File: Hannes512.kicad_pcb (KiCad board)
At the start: 2 copper layers, 54.3 x 72.2 mm, 23 parts, among them J0 TED_SOCKET, J1 CONN_CS, J2 RAM_SELECTOR, U1 MOS_7360_TED, U2 AS6C4008, U3 74HCT02, U4 NE555, U5 74HCT573, U6 74HCT245, U7 GAL20V8

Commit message: Hannes256 -> Hannes512
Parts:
- J0: footprint Hannes256:DIP-48_W15.24mm_LongPads_ModSilkS -> Hannes512:DIP-48_W15.24mm_LongPads_ModSilkS
- V1: footprint Hannes256:cc_by_nc_sa -> Hannes512:cc_by_nc_sa
- V2: footprint Hannes256:logo -> Hannes512:logo
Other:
- board text added: "CC-BY-NC-SA © SukkoPera 2022-2023 github.com/ SukkoPera/ Hannes512"
- board text removed: "CC-BY-NC-SA © SukkoPera 2022-2023 github.com/ SukkoPera/ Hannes256"

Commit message: Ready for V1
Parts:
- C5, C6: moved to F.Cu
- U5, U6: footprint Package_SO:SOIC-20W_7.5x12.8mm_P1.27mm -> Package_SO:SO-20_5.3x12.6mm_P1.27mm
- moved V1 10.5 mm to (148.5, 128.3)
- moved C5 3.08 mm to (112.5, 81.7)
- moved C6 3.08 mm to (107.7, 81.7), turned to 0 degrees
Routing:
- net d1: track 82.8 -> 78.0 mm
- net d2: track 84.1 -> 79.8 mm
- net a16: track 72.4 -> 76.1 mm
- net +5V: track 237.2 -> 233.9 mm, vias 10 -> 9
- net a7: track 25.6 -> 28.1 mm
- net d6: track 72.5 -> 70.0 mm
- net d3: track 62.7 -> 60.2 mm
- net d4: track 64.9 -> 62.5 mm
- net d7: track 78.8 -> 76.4 mm
- net d5: track 68.9 -> 66.5 mm
- net a10: track 41.9 -> 44.3 mm
- net d0: track 79.0 -> 76.6 mm
- net /~RAS~/~CAS~ Generation/~cs_ramrd: track 57.7 -> 55.6 mm
- net a15: track 44.5 -> 46.6 mm
- net p6: track 46.6 -> 44.6 mm
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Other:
- board text added: "CC-BY-NC-SA © SukkoPera 2023 github.com/ SukkoPera/ Hannes512"
- board text added: "V1"
- board text removed: "CC-BY-NC-SA © SukkoPera 2022-2023 github.com/ SukkoPera/ Hannes512"
- board text removed: "V4"

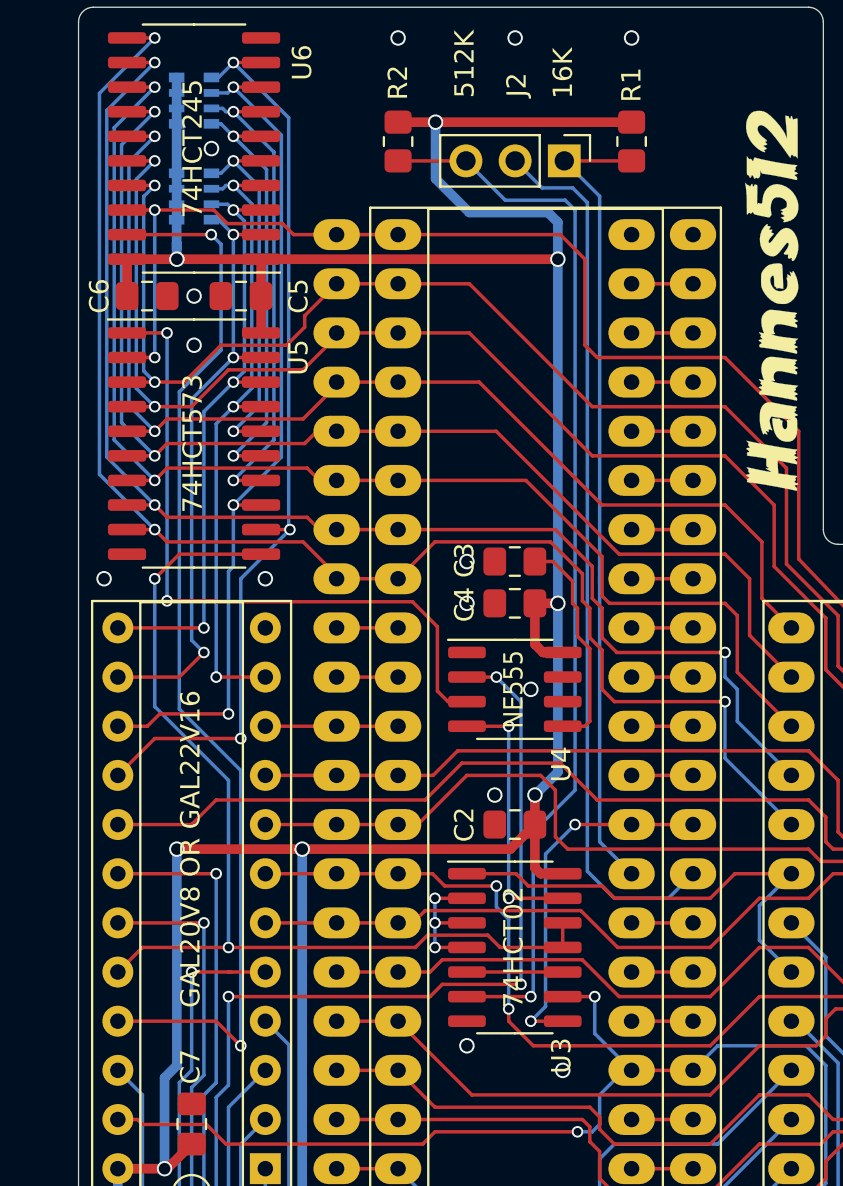
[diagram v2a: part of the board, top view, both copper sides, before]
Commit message: Some rerouting
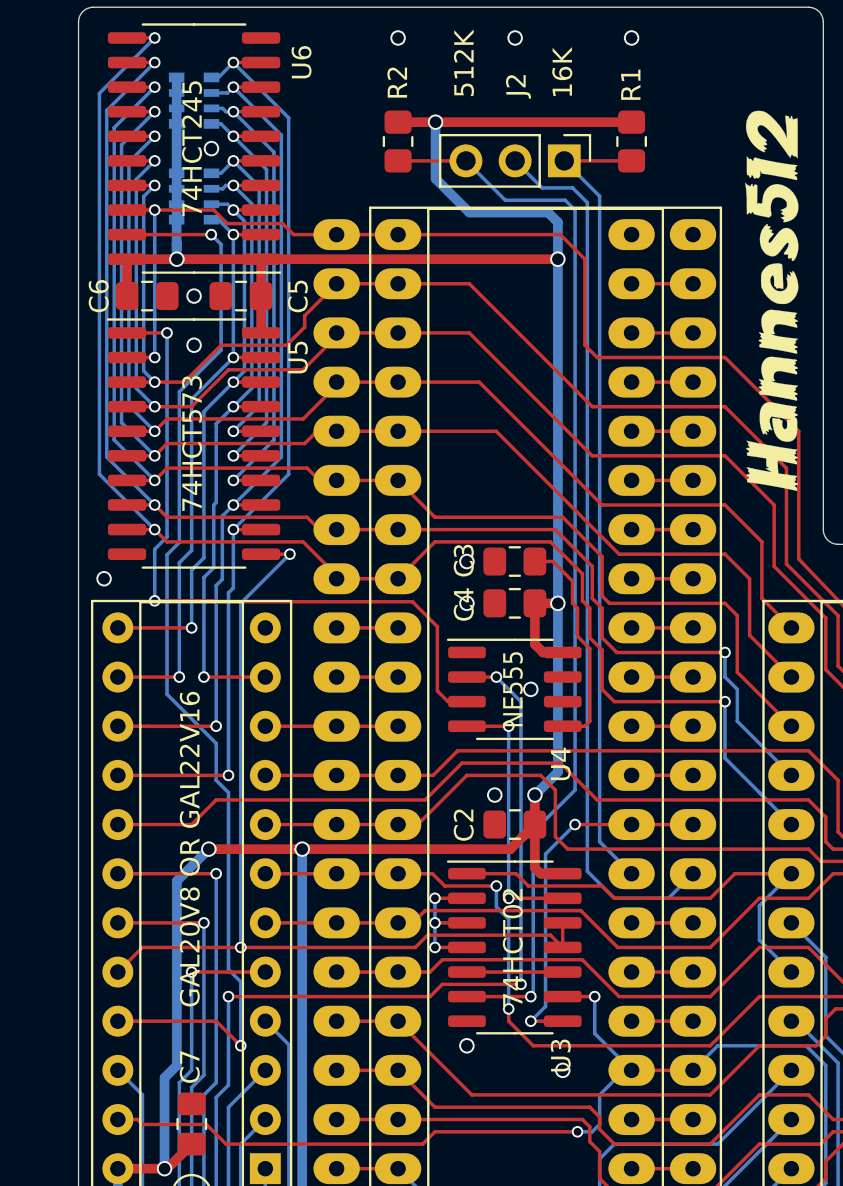
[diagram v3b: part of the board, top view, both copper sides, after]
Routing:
- net /~RAS~/~CAS~ Generation/cs_ramwr: track 52.0 -> 48.2 mm
- net +5V: track 233.9 -> 232.9 mm
- net /~RAS~/~CAS~ Generation/~u3enable: track 36.1 -> 37.0 mm
- net p2: track 33.2 -> 34.1 mm
- net p7: track 48.7 -> 49.3 mm
- net /~RAS~/~CAS~ Generation/~cs_ramrd: track 55.6 -> 56.1 mm
- net p0: track 32.0 -> 31.5 mm
- net GND: vias 26 -> 25

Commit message: More rerouting
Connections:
- net Net-(U3-Pad13) renamed /~RAS~/~CAS~ Generation/~cs_ramwr
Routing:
- net d0: track 76.6 -> 74.0 mm
- net /~RAS~/~CAS~ Generation/~cs_ramrd: track 56.1 -> 53.6 mm
- net +5V: track 232.9 -> 235.0 mm

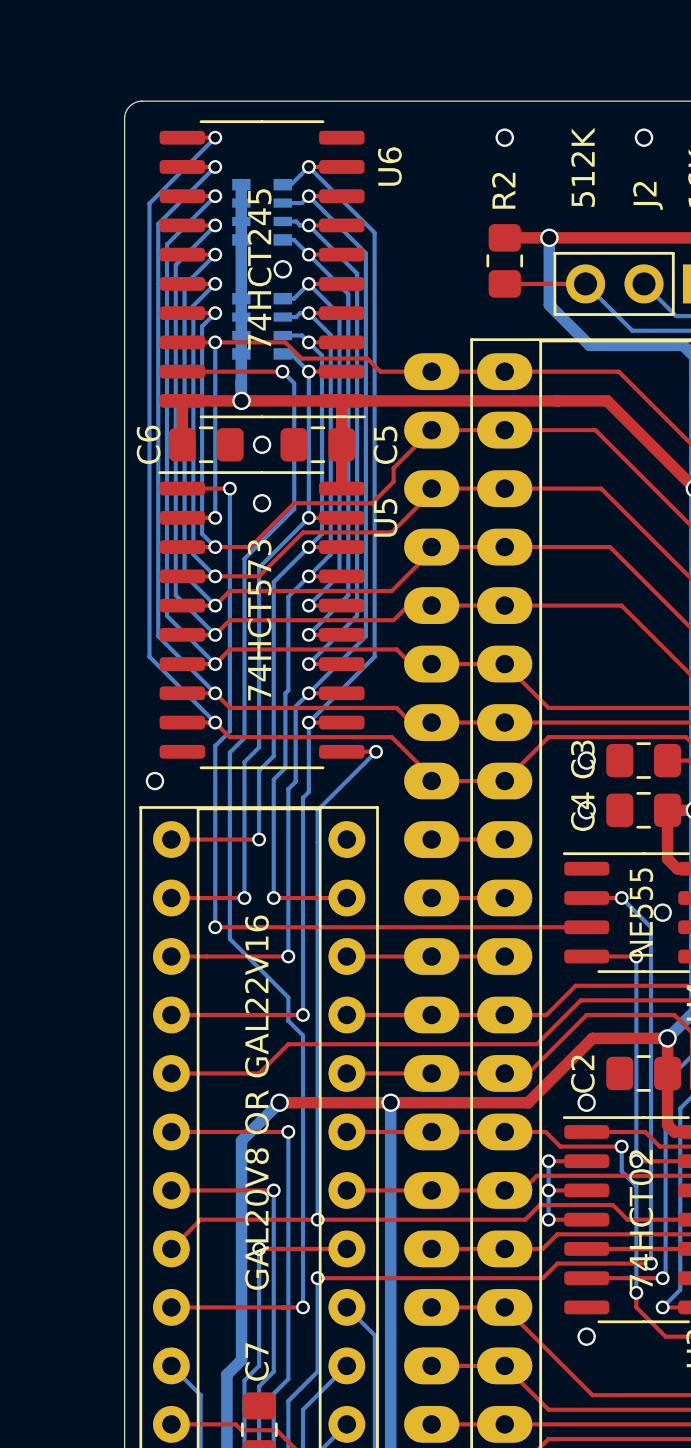
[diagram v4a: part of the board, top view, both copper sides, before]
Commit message: Relocate RN1/2 on top
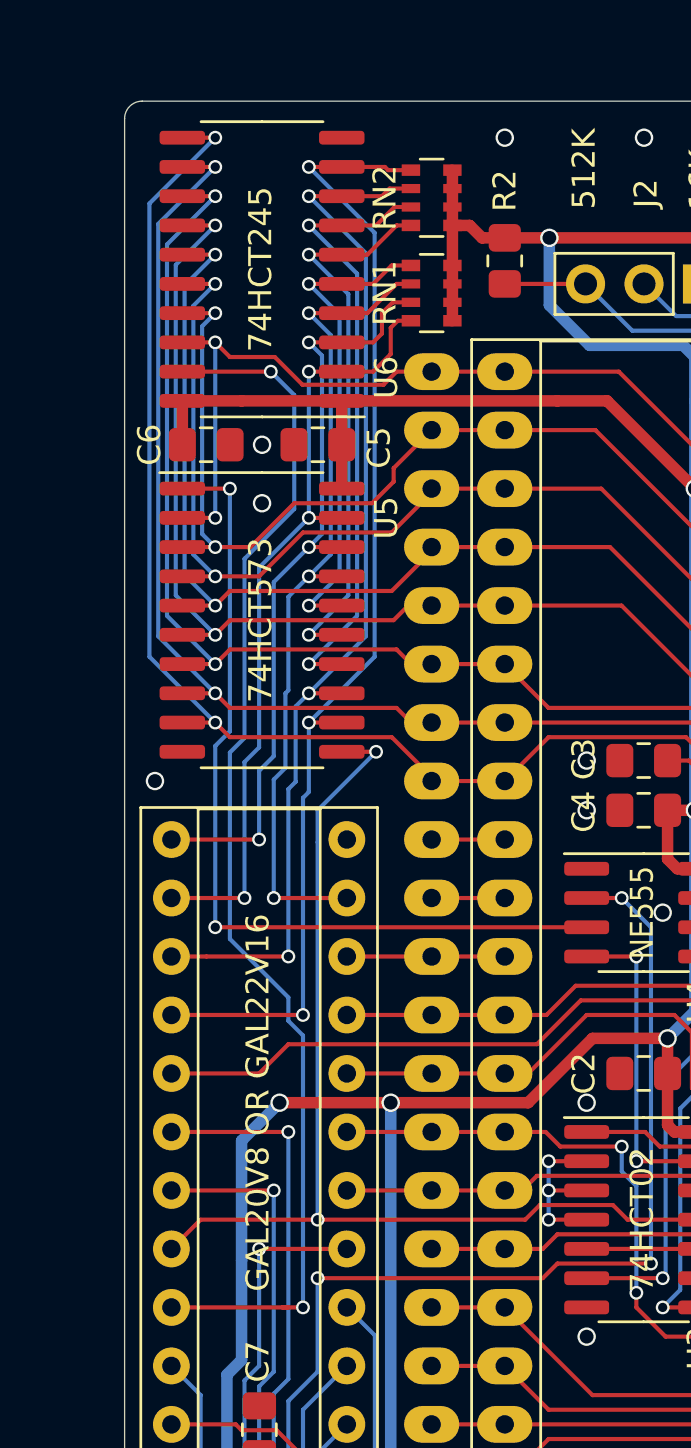
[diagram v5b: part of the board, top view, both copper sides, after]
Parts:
- RN1, RN2: moved to F.Cu
- moved RN1 7.51 mm to (117.5, 75.1), turned to 0 degrees
- moved RN2 7.39 mm to (117.5, 70.9), turned to 0 degrees
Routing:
- net p0: track 31.5 -> 34.6 mm
- net p1: track 30.9 -> 33.9 mm
- net p2: track 34.1 -> 36.4 mm
- net p5: track 24.9 -> 27.0 mm
- net p4: track 22.2 -> 24.3 mm
- net p3: track 19.3 -> 21.3 mm
- net p6: track 44.6 -> 46.5 mm
- net p7: track 49.3 -> 50.9 mm
- net +5V: track 235.0 -> 234.3 mm, vias 9 -> 8
- net GND: vias 25 -> 24

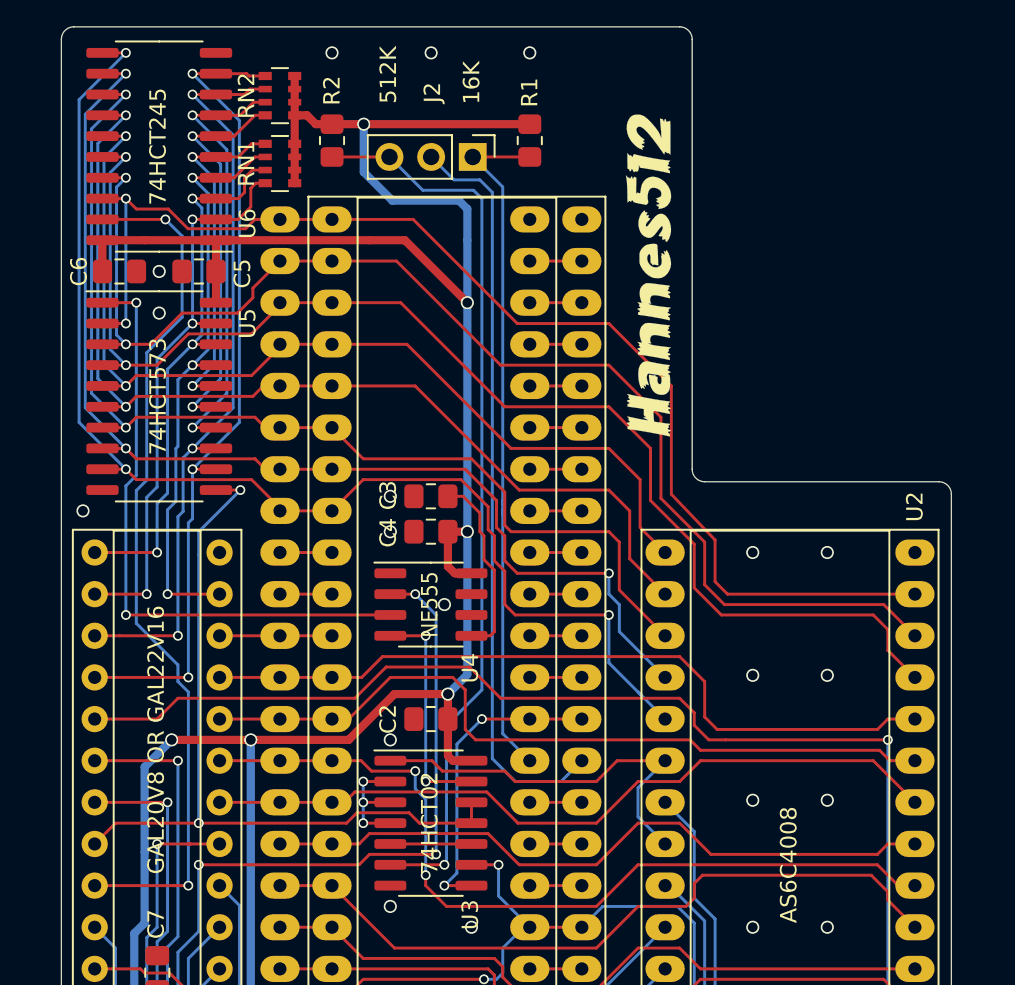
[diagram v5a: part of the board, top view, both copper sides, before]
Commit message: Add TED Kx Protection
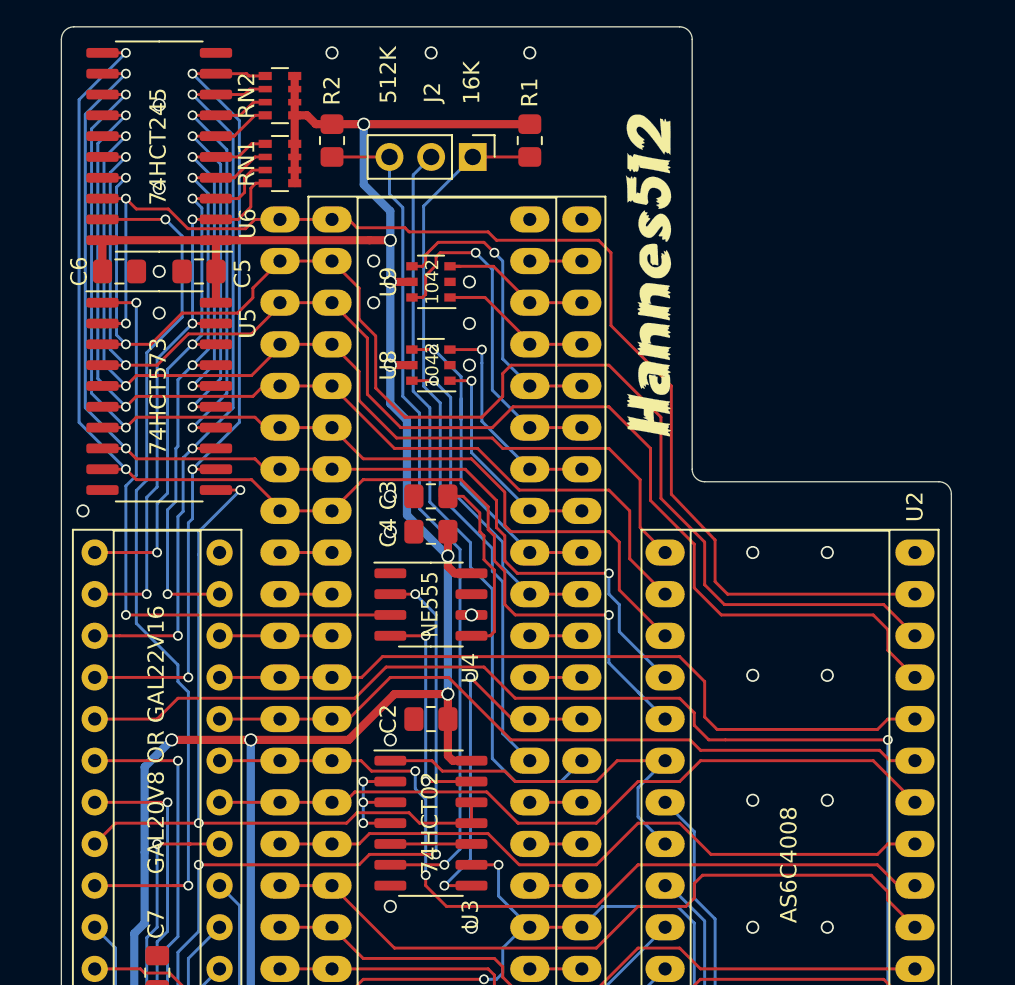
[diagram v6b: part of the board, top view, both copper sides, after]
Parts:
- added U8: DT1042, Package_SO:TSOP-6_1.65x3.05mm_P0.95mm, F.Cu at (126.7, 87.4)
- added U9: DT1042, Package_SO:TSOP-6_1.65x3.05mm_P0.95mm, F.Cu at (126.7, 82.3)
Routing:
- net /k4: track 3.17 -> 21.2 mm, vias 0 -> 1
- net /k1: track 3.17 -> 20.6 mm, vias 0 -> 1
- net /k0: track 3.17 -> 20.0 mm, vias 0 -> 1
- net /k5: track 3.17 -> 18.4 mm, vias 0 -> 1
- net /k2: track 3.17 -> 13.8 mm, vias 0 -> 1
- net /k3: track 3.17 -> 13.7 mm, vias 0 -> 1
- net +5V: track 234.3 -> 226.3 mm, vias 8 -> 10
- net d1: track 78.0 -> 84.4 mm
- net /k7: track 3.17 -> 9.58 mm
- net /k6: track 3.17 -> 9.30 mm
- net CLKOUT: track 18.9 -> 22.9 mm
- net d2: track 79.8 -> 82.9 mm
- net ~CAS_64K: track 55.1 -> 52.2 mm
- net d0: track 74.5 -> 77.1 mm
- net /~cas_16k: track 42.4 -> 44.2 mm
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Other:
- board text added: "1042"
- board text added: "512kB RAM Expansion for the Commodore 16 Based on work by Hannes and Solder/Synergy Thanks to TLC and eslapion!"
- board text removed: "512kB RAM Expansion for the Commodore 16 Based on work by Hannes and Solder/Synergy Thanks to TLC and eslapion"

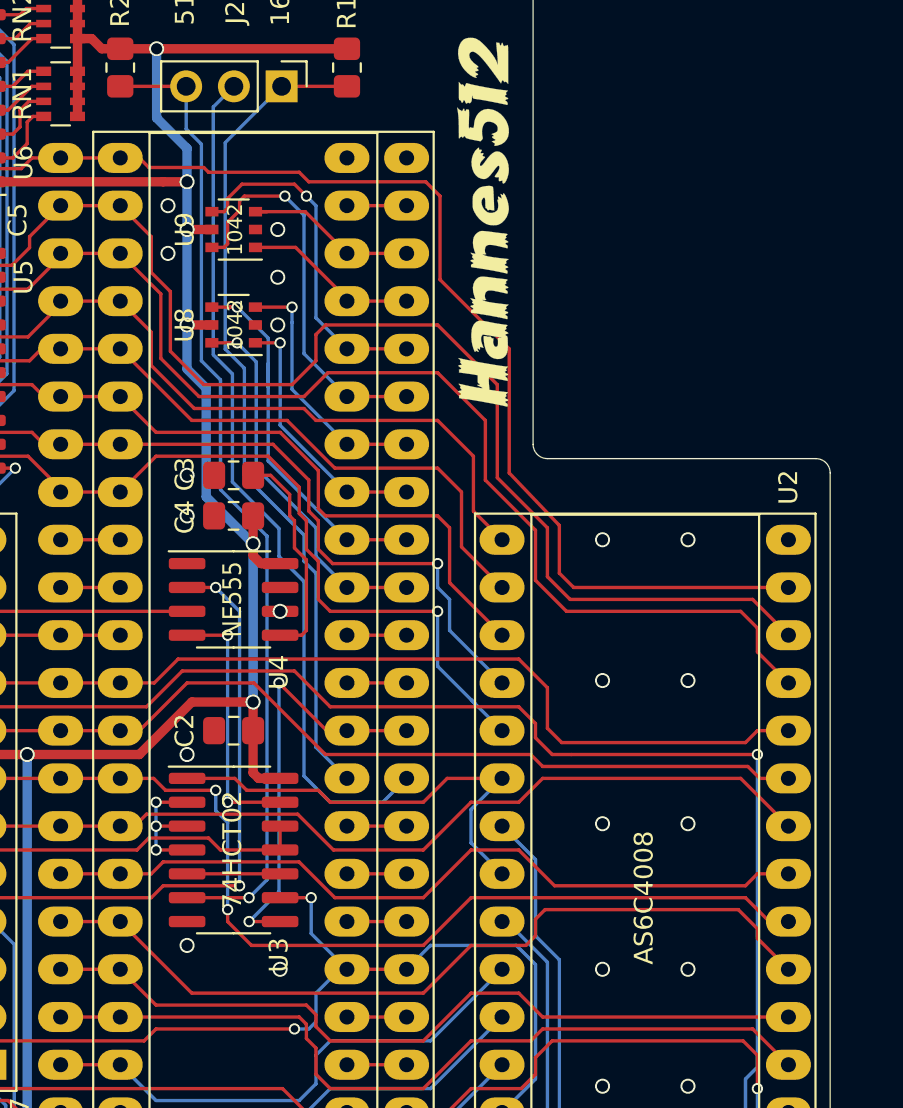
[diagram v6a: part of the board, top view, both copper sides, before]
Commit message: Ground plane improvements
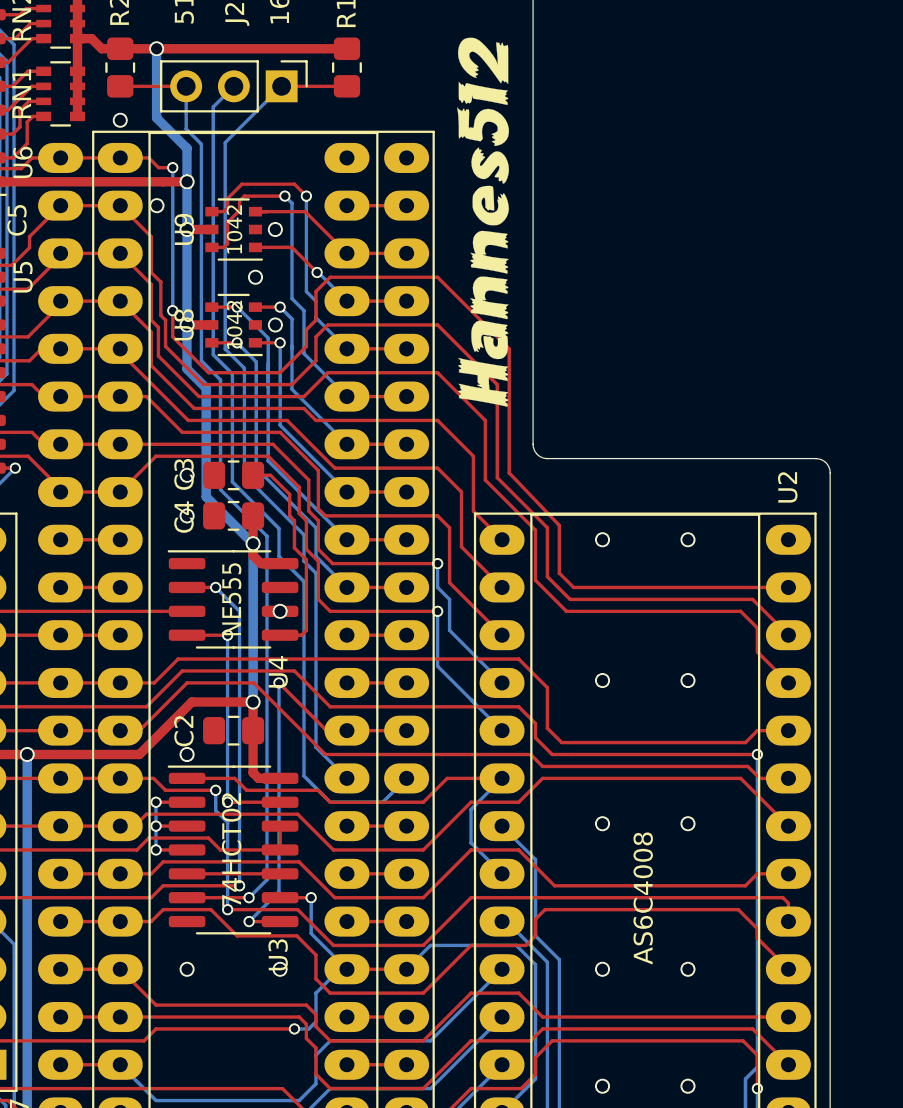
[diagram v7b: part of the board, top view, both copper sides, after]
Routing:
- net d0: track 77.1 -> 85.4 mm, vias 2 -> 4
- net a10: track 44.3 -> 45.6 mm
- net /k6: track 9.30 -> 9.35 mm, vias 0 -> 1
